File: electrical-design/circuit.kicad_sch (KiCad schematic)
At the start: 52 parts, among them J1 AVR-ISP-6, Q1 2N3906, Q2 2N3906, Q3 2N3906, Q4 2N3906, SW1 Reset Button, SW2 DS02C-254-1L-04BE, SW3 Reset Button, U1 ATmega8A-P, U2 LTC-4627JR, U3 NE555P, Y1 16MHz

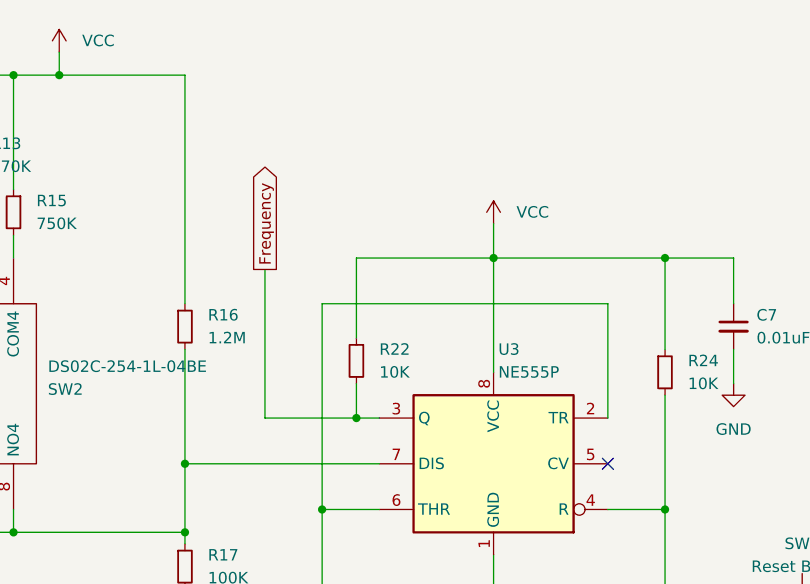
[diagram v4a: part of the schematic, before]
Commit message: Added Input Protection on NE555 Timer
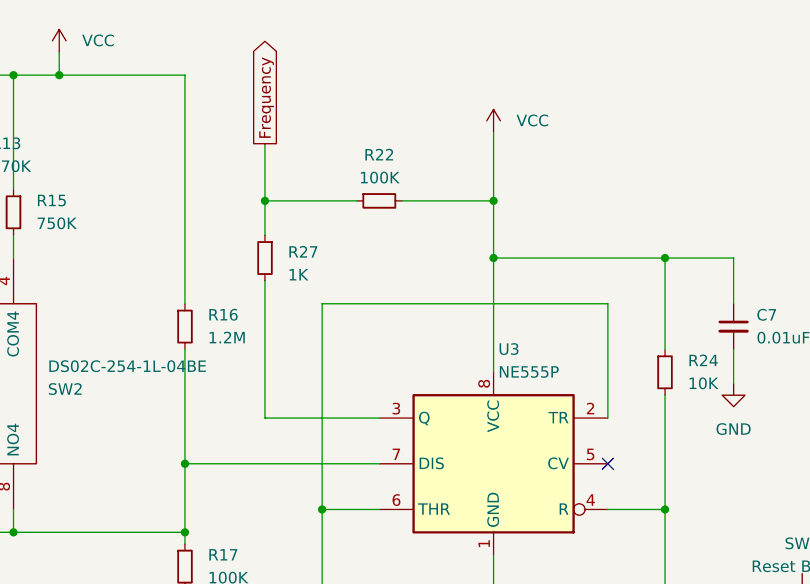
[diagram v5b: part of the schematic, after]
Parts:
- added R27: 1K, Resistor_THT:R_Axial_DIN0207_L6.3mm_D2.5mm_P7.62mm_Horizontal, symbol Device:R_Small
- R22: value 10K -> 100K
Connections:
- net Frequency: now also R22.1, R27.1; no longer R22.2, U3.3 (Q)
- net VCC: now also R22.2; no longer R22.1
- new net: R27.2, U3.3 (Q)
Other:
- moved on the sheet: R22
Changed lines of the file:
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@@
   (junction (at 48.26 85.09) (diameter 0) (color 0 0 0 0)
   )
+  (junction (at 189.23 33.02) (diameter 0) (color 0 0 0 0)
+  )
   (junction (at 214.63 39.37) (diameter 0) (color 0 0 0 0)
   )
@@
   (junction (at 33.02 59.69) (diameter 0) (color 0 0 0 0)
   )
-  (junction (at 199.39 57.15) (diameter 0) (color 0 0 0 0)
-  )
   (junction (at 54.61 41.91) (diameter 0) (color 0 0 0 0)
+  )
+  (junction (at 214.63 33.02) (diameter 0) (color 0 0 0 0)
   )
   (junction (at 74.93 107.95) (diameter 0) (color 0 0 0 0)
@@
     (stroke (width 0) (type default))
   )
-  (wire (pts (xy 199.39 57.15) (xy 201.93 57.15))
+  (wire (pts (xy 189.23 57.15) (xy 201.93 57.15))
     (stroke (width 0) (type default))
   )
@@
     (stroke (width 0) (type default))
   )
-  (wire (pts (xy 189.23 40.64) (xy 189.23 57.15))
-    (stroke (width 0) (type default))
-  )
   (wire (pts (xy 118.11 72.39) (xy 118.11 76.2))
     (stroke (width 0) (type default))
@@
     (stroke (width 0) (type default))
   )
+  (wire (pts (xy 189.23 41.91) (xy 189.23 57.15))
+    (stroke (width 0) (type default))
+  )
   (wire (pts (xy 54.61 41.91) (xy 59.69 41.91))
     (stroke (width 0) (type default))
@@
     (stroke (width 0) (type default))
   )
-  (wire (pts (xy 199.39 39.37) (xy 214.63 39.37))
-    (stroke (width 0) (type default))
-  )
   (wire (pts (xy 259.08 144.78) (xy 259.08 130.81))
     (stroke (width 0) (type default))
@@
     (stroke (width 0) (type default))
   )
-  (wire (pts (xy 199.39 48.26) (xy 199.39 39.37))
-    (stroke (width 0) (type default))
-  )
   (wire (pts (xy 139.7 46.99) (xy 144.78 46.99))
     (stroke (width 0) (type default))
@@
     (stroke (width 0) (type default))
   )
+  (wire (pts (xy 189.23 26.67) (xy 189.23 33.02))
+    (stroke (width 0) (type default))
+  )
   (wire (pts (xy 90.17 64.77) (xy 95.25 64.77))
     (stroke (width 0) (type default))
@@
     (stroke (width 0) (type default))
   )
-  (wire (pts (xy 214.63 35.56) (xy 214.63 39.37))
+  (wire (pts (xy 214.63 25.4) (xy 214.63 33.02))
     (stroke (width 0) (type default))
   )
@@
     (stroke (width 0) (type default))
   )
+  (wire (pts (xy 204.47 33.02) (xy 214.63 33.02))
+    (stroke (width 0) (type default))
+  )
   (wire (pts (xy 33.02 46.99) (xy 33.02 59.69))
     (stroke (width 0) (type default))
@@
     (stroke (width 0) (type default))
   )
+  (wire (pts (xy 189.23 33.02) (xy 199.39 33.02))
+    (stroke (width 0) (type default))
+  )
   (wire (pts (xy 24.13 73.66) (xy 24.13 85.09))
     (stroke (width 0) (type default))
@@
     (stroke (width 0) (type default))
   )
-  (wire (pts (xy 199.39 53.34) (xy 199.39 57.15))
-    (stroke (width 0) (type default))
-  )
   (wire (pts (xy 273.05 107.95) (xy 273.05 124.46))
     (stroke (width 0) (type default))
@@
     (stroke (width 0) (type default))
   )
-  (wire (pts (xy 189.23 57.15) (xy 199.39 57.15))
-    (stroke (width 0) (type default))
-  )
   (wire (pts (xy 241.3 49.53) (xy 241.3 53.34))
     (stroke (width 0) (type default))
@@
     (stroke (width 0) (type default))
   )
+  (wire (pts (xy 214.63 33.02) (xy 214.63 39.37))
+    (stroke (width 0) (type default))
+  )
   (wire (pts (xy 248.92 107.95) (xy 248.92 115.57))
+    (stroke (width 0) (type default))
+  )
+  (wire (pts (xy 189.23 33.02) (xy 189.23 36.83))
     (stroke (width 0) (type default))
   )
@@
     )
   )
-  (global_label "Frequency" (shape output) (at 189.23 40.64 90) (fields_autoplaced)
+  (global_label "Frequency" (shape output) (at 189.23 26.67 90) (fields_autoplaced)
     (effects (font (size 1.27 1.27)) (justify left))
-    (property "Intersheetrefs" "${INTERSHEET_REFS}" (at 189.3094 28.6717 90)
+    (property "Intersheetrefs" "${INTERSHEET_REFS}" (at 189.3094 14.7017 90)
       (effects (font (size 1.27 1.27)) (justify left) hide)
     )
@@
     )
   )
-  (symbol (lib_id "Device:R_Small") (at 199.39 50.8 0) (mirror y) (unit 1)
-    (in_bom yes) (on_board yes) (dnp no) (fields_autoplaced)
-    (property "Reference" "R22" (at 201.93 49.5299 0)
-      (effects (font (size 1.27 1.27)) (justify right))
-    )
-    (property "Value" "10K" (at 201.93 52.0699 0)
-      (effects (font (size 1.27 1.27)) (justify right))
-    )
-    (property "Footprint" "Resistor_THT:R_Axial_DIN0207_L6.3mm_D2.5mm_P7.62mm_Horizontal" (at 199.39 50.8 0)
-      (effects (font (size 1.27 1.27)) hide)
-    )
-    (property "Datasheet" "~" (at 199.39 50.8 0)
+  (symbol (lib_id "Device:R_Small") (at 201.93 33.02 90) (mirror x) (unit 1)
+    (in_bom yes) (on_board yes) (dnp no) (fields_autoplaced)
+    (property "Reference" "R22" (at 201.93 27.94 90)
+      (effects (font (size 1.27 1.27)))
+    )
+    (property "Value" "100K" (at 201.93 30.48 90)
+      (effects (font (size 1.27 1.27)))
+    )
+    (property "Footprint" "Resistor_THT:R_Axial_DIN0207_L6.3mm_D2.5mm_P7.62mm_Horizontal" (at 201.93 33.02 0)
+      (effects (font (size 1.27 1.27)) hide)
+    )
+    (property "Datasheet" "~" (at 201.93 33.02 0)
       (effects (font (size 1.27 1.27)) hide)
     )
@@
     )
   )
-  (symbol (lib_id "power:VCC") (at 214.63 35.56 0) (unit 1)
-    (in_bom yes) (on_board yes) (dnp no) (fields_autoplaced)
-    (property "Reference" "#PWR013" (at 214.63 39.37 0)
-      (effects (font (size 1.27 1.27)) hide)
-    )
-    (property "Value" "VCC" (at 217.17 34.2899 0)
-      (effects (font (size 1.27 1.27)) (justify left))
-    )
-    (property "Footprint" "" (at 214.63 35.56 0)
-      (effects (font (size 1.27 1.27)) hide)
-    )
-    (property "Datasheet" "" (at 214.63 35.56 0)
+  (symbol (lib_id "power:VCC") (at 214.63 25.4 0) (unit 1)
+    (in_bom yes) (on_board yes) (dnp no) (fields_autoplaced)
+    (property "Reference" "#PWR013" (at 214.63 29.21 0)
+      (effects (font (size 1.27 1.27)) hide)
+    )
+    (property "Value" "VCC" (at 217.17 24.1299 0)
+      (effects (font (size 1.27 1.27)) (justify left))
+    )
+    (property "Footprint" "" (at 214.63 25.4 0)
+      (effects (font (size 1.27 1.27)) hide)
+    )
+    (property "Datasheet" "" (at 214.63 25.4 0)
       (effects (font (size 1.27 1.27)) hide)
     )
@@
         )
       )
+    )
+  )
+  (symbol (lib_id "Device:R_Small") (at 189.23 39.37 0) (mirror y) (unit 1)
+    (in_bom yes) (on_board yes) (dnp no) (fields_autoplaced)
+    (property "Reference" "R27" (at 191.77 38.735 0)
+      (effects (font (size 1.27 1.27)) (justify right))
+    )
+    (property "Value" "1K" (at 191.77 41.275 0)
+      (effects (font (size 1.27 1.27)) (justify right))
+    )
+    (property "Footprint" "Resistor_THT:R_Axial_DIN0207_L6.3mm_D2.5mm_P7.62mm_Horizontal" (at 189.23 39.37 0)
+      (effects (font (size 1.27 1.27)) hide)
+    )
+    (property "Datasheet" "~" (at 189.23 39.37 0)
+      (effects (font (size 1.27 1.27)) hide)
+    )
+    (pin "1")
+    (pin "2")
+    (instances
+      (project "circuit"
+        (path "/e92f8e40-1e47-4cd0-a865-c589067a003b"
+          (reference "R27") (unit 1)
+        )
+      )

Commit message: Completed Design of 1.2
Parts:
- removed SW2: DS02C-254-1L-04BE, DIP Switch:DS02C2541L04BE, symbol DIP Switch:DS02C-254-1L-04BE
- added SW2: SW_DIP_x04, Button_Switch_THT:SW_DIP_SPSTx04_Slide_9.78x12.34mm_W7.62mm_P2.54mm, symbol Switch:SW_DIP_x04
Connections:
- net at R13.2: now also SW2.2
- net at R15.2: now also SW2.4
- net at R12.2: now also SW2.1
- net at R14.2: now also SW2.3
- net at R16.2, R17.1, U3.7 (DIS): now also SW2.5, SW2.6, SW2.7, SW2.8
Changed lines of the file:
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@@
     (stroke (width 0) (type default))
   )
-  (wire (pts (xy 156.21 30.48) (xy 156.21 39.37))
+  (wire (pts (xy 156.21 30.48) (xy 156.21 44.45))
     (stroke (width 0) (type default))
   )
@@
     (stroke (width 0) (type default))
   )
-  (wire (pts (xy 153.67 30.48) (xy 153.67 39.37))
+  (wire (pts (xy 153.67 30.48) (xy 153.67 44.45))
     (stroke (width 0) (type default))
   )
@@
     (stroke (width 0) (type default))
   )
-  (wire (pts (xy 161.29 67.31) (xy 161.29 69.85))
+  (wire (pts (xy 161.29 59.69) (xy 161.29 69.85))
     (stroke (width 0) (type default))
   )
@@
     (stroke (width 0) (type default))
   )
-  (wire (pts (xy 153.67 67.31) (xy 153.67 69.85))
+  (wire (pts (xy 153.67 59.69) (xy 153.67 69.85))
     (stroke (width 0) (type default))
   )
@@
     (stroke (width 0) (type default))
   )
-  (wire (pts (xy 158.75 67.31) (xy 158.75 69.85))
+  (wire (pts (xy 158.75 59.69) (xy 158.75 69.85))
     (stroke (width 0) (type default))
   )
@@
     (stroke (width 0) (type default))
   )
-  (wire (pts (xy 158.75 36.83) (xy 158.75 39.37))
+  (wire (pts (xy 158.75 36.83) (xy 158.75 44.45))
     (stroke (width 0) (type default))
   )
@@
     (stroke (width 0) (type default))
   )
-  (wire (pts (xy 156.21 67.31) (xy 156.21 69.85))
+  (wire (pts (xy 156.21 59.69) (xy 156.21 69.85))
     (stroke (width 0) (type default))
   )
@@
     (stroke (width 0) (type default))
   )
-  (wire (pts (xy 161.29 36.83) (xy 161.29 39.37))
+  (wire (pts (xy 161.29 36.83) (xy 161.29 44.45))
     (stroke (width 0) (type default))
   )
@@
     )
   )
-  (symbol (lib_id "DIP Switch:DS02C-254-1L-04BE") (at 153.67 39.37 90) (mirror x) (unit 1)
-    (in_bom yes) (on_board yes) (dnp no)
-    (property "Reference" "SW2" (at 165.1 53.975 90)
-      (effects (font (size 1.27 1.27)) (justify right))
-    )
-    (property "Value" "DS02C-254-1L-04BE" (at 165.1 51.435 90)
-      (effects (font (size 1.27 1.27)) (justify right))
-    )
-    (property "Footprint" "DIP Switch:DS02C2541L04BE" (at 151.13 63.5 0)
-      (effects (font (size 1.27 1.27)) (justify left) hide)
-    )
-    (property "Datasheet" "https://www.cuidevices.com/product/resource/digikeypdf/ds02-254.pdf" (at 153.67 63.5 0)
-      (effects (font (size 1.27 1.27)) (justify left) hide)
-    )
-    (property "Description" "DIP Switches / SIP Switches DIP Switch, SPST, 2.54 pitch, Raised actuator, convex bottom, long pin, 4 position, Blue" (at 156.21 63.5 0)
-      (effects (font (size 1.27 1.27)) (justify left) hide)
-    )
-    (property "Height" "9.9" (at 158.75 63.5 0)
-      (effects (font (size 1.27 1.27)) (justify left) hide)
-    )
-    (property "Mouser Part Number" "490-DS02C-254-1L04BE" (at 161.29 63.5 0)
-      (effects (font (size 1.27 1.27)) (justify left) hide)
-    )
-    (property "Mouser Price/Stock" "https://www.mouser.co.uk/ProductDetail/CUI-Devices/DS02C-254-1L-04BE?qs=wnTfsH77Xs4EGXqmfKoj6A%3D%3D" (at 163.83 63.5 0)
-      (effects (font (size 1.27 1.27)) (justify left) hide)
-    )
-    (property "Manufacturer_Name" "CUI Devices" (at 166.37 63.5 0)
-      (effects (font (size 1.27 1.27)) (justify left) hide)
-    )
-    (property "Manufacturer_Part_Number" "DS02C-254-1L-04BE" (at 168.91 63.5 0)
-      (effects (font (size 1.27 1.27)) (justify left) hide)
-    )
-    (pin "1")
-    (pin "2")
-    (pin "3")
-    (pin "4")
-    (pin "5")
-    (pin "6")
-    (pin "7")
-    (pin "8")
-    (instances
-      (project "circuit"
-        (path "/e92f8e40-1e47-4cd0-a865-c589067a003b"
-          (reference "SW2") (unit 1)
-        )
-      )
-    )
-  )
   (symbol (lib_id "Device:R_Small") (at 180.34 73.66 0) (unit 1)
     (in_bom yes) (on_board yes) (dnp no) (fields_autoplaced)
@@
         )
       )
+    )
+  )
+  (symbol (lib_id "Switch:SW_DIP_x04") (at 158.75 52.07 90) (mirror x) (unit 1)
+    (in_bom yes) (on_board yes) (dnp no) (fields_autoplaced)
+    (property "Reference" "SW2" (at 165.1 51.435 90)
+      (effects (font (size 1.27 1.27)) (justify right))
+    )
+    (property "Value" "SW_DIP_x04" (at 165.1 53.975 90)
+      (effects (font (size 1.27 1.27)) (justify right))
+    )
+    (property "Footprint" "Button_Switch_THT:SW_DIP_SPSTx04_Slide_9.78x12.34mm_W7.62mm_P2.54mm" (at 158.75 52.07 0)
+      (effects (font (size 1.27 1.27)) hide)
+    )
+    (property "Datasheet" "~" (at 158.75 52.07 0)
+      (effects (font (size 1.27 1.27)) hide)
+    )
+    (pin "1")
+    (pin "2")
+    (pin "3")
+    (pin "4")
+    (pin "5")
+    (pin "6")
+    (pin "7")
+    (pin "8")
+    (instances
+      (project "circuit"
+        (path "/e92f8e40-1e47-4cd0-a865-c589067a003b"
+          (reference "SW2") (unit 1)
+        )
+      )

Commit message: Made DIP Packages Use Socket
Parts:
- U1: footprint Package_DIP:DIP-28_W7.62mm -> Package_DIP:DIP-28_W7.62mm_Socket
- U3: footprint Package_DIP:DIP-8_W7.62mm -> Package_DIP:DIP-8_W7.62mm_Socket
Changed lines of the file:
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@@
       (effects (font (size 1.27 1.27)) (justify left))
     )
-    (property "Footprint" "Package_DIP:DIP-28_W7.62mm" (at 74.93 69.85 0)
+    (property "Footprint" "Package_DIP:DIP-28_W7.62mm_Socket" (at 74.93 69.85 0)
       (effects (font (size 1.27 1.27) italic) hide)
     )
@@
       (effects (font (size 1.27 1.27)) (justify right))
     )
-    (property "Footprint" "Package_DIP:DIP-8_W7.62mm" (at 198.12 72.39 0)
-      (effects (font (size 1.27 1.27)) hide)
-    )
+    (property "Footprint" "Package_DIP:DIP-8_W7.62mm_Socket" (at 198.12 72.39 0)
+      (effects (font (size 1.27 1.27)) hide)
+    )
